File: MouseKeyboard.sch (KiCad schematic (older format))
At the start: 16 parts, among them IC1 ATMEGA328P-P, J1 USB, SW1 SW_PUSH, SW2 SW_PUSH, SW3 SW_PUSH, SW4 SW_PUSH, SW5 SW_PUSH, SW6 SW_PUSH, SW7 SW_PUSH

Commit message: Net File
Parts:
- R1: value R -> 2K2
- R2, R3: value R -> 68R
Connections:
- net +5V: now also IC1.20 (AVCC), IC1.7 (VCC), J1.1 (Vbus)
- net GND: no longer IC1.22 (GND), IC1.8 (GND)
- net at J1.3 (D+): now also D2.2 (K), R2.1
- no-connect marks 0 -> 17
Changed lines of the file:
@@
 EELAYER 24 0
 EELAYER END
-$Descr A4 11693 8268
+$Descr A 11000 8500
 encoding utf-8
 Sheet 1 1
-Title ""
-Date ""
+Title "Arduino Mouse Keyboard"
+Date "12 Feb 2015"
 Rev ""
 Comp ""
@@
 $EndComp
 $Comp
-L +5V #PWR6
-U 1 1 54DAA8BA
-P 9450 3400
-F 0 "#PWR6" H 9450 3490 20  0001 C CNN
-F 1 "+5V" H 9450 3490 30  0000 C CNN
-F 2 "" H 9450 3400 60  0000 C CNN
-F 3 "" H 9450 3400 60  0000 C CNN
-	1    9450 3400
-	1    0    0    -1
-$EndComp
-$Comp
-L +5V #PWR2
+L +5V #PWR01
 U 1 1 54DAA9EC
 P 1250 7150
-F 0 "#PWR2" H 1250 7240 20  0001 C CNN
+F 0 "#PWR01" H 1250 7240 20  0001 C CNN
 F 1 "+5V" H 1250 7240 30  0000 C CNN
 F 2 "" H 1250 7150 60  0000 C CNN
@@
 	1    1250 7150
 	0    -1   -1   0
-$EndComp
-$Comp
-L GND #PWR3
-U 1 1 54DAAA0D
-P 3850 7350
-F 0 "#PWR3" H 3850 7350 30  0001 C CNN
-F 1 "GND" H 3850 7280 30  0001 C CNN
-F 2 "" H 3850 7350 60  0000 C CNN
-F 3 "" H 3850 7350 60  0000 C CNN
-	1    3850 7350
-	1    0    0    -1
 $EndComp
 $Comp
@@
 $EndComp
 $Comp
-L GND #PWR1
-U 1 1 54DD39B5
-P 1200 5750
-F 0 "#PWR1" H 1200 5750 30  0001 C CNN
-F 1 "GND" H 1200 5680 30  0001 C CNN
-F 2 "" H 1200 5750 60  0000 C CNN
-F 3 "" H 1200 5750 60  0000 C CNN
-	1    1200 5750
-	1    0    0    -1
-$EndComp
-$Comp
 L USB J1
 U 1 1 54DD5132
@@
 P 6400 1900
 F 0 "R3" V 6480 1900 40  0000 C CNN
-F 1 "R" V 6407 1901 40  0000 C CNN
+F 1 "68R" V 6407 1901 40  0000 C CNN
 F 2 "" V 6330 1900 30  0000 C CNN
 F 3 "" H 6400 1900 30  0000 C CNN
@@
 P 6400 1650
 F 0 "R2" V 6480 1650 40  0000 C CNN
-F 1 "R" V 6407 1651 40  0000 C CNN
+F 1 "68R" V 6407 1651 40  0000 C CNN
 F 2 "" V 6330 1650 30  0000 C CNN
 F 3 "" H 6400 1650 30  0000 C CNN
@@
 $EndComp
 $Comp
-L +5V #PWR5
+L +5V #PWR02
 U 1 1 54DD56D2
 P 5850 1100
-F 0 "#PWR5" H 5850 1190 20  0001 C CNN
+F 0 "#PWR02" H 5850 1190 20  0001 C CNN
 F 1 "+5V" H 5850 1190 30  0000 C CNN
 F 2 "" H 5850 1100 60  0000 C CNN
@@
 P 5850 1400
 F 0 "R1" V 5930 1400 40  0000 C CNN
-F 1 "R" V 5857 1401 40  0000 C CNN
+F 1 "2K2" V 5857 1401 40  0000 C CNN
 F 2 "" V 5780 1400 30  0000 C CNN
 F 3 "" H 5850 1400 30  0000 C CNN
@@
 $EndComp
 $Comp
-L GND #PWR4
+L GND #PWR03
 U 1 1 54DD5A19
 P 5200 2550
-F 0 "#PWR4" H 5200 2550 30  0001 C CNN
+F 0 "#PWR03" H 5200 2550 30  0001 C CNN
 F 1 "GND" H 5200 2480 30  0001 C CNN
 F 2 "" H 5200 2550 60  0000 C CNN
@@
 Connection ~ 2200 7150
 Wire Wire Line
-	3850 6450 3850 7350
-Wire Wire Line
 	2700 6450 2700 7000
-Wire Wire Line
-	2700 7000 3850 7000
-Connection ~ 3850 7000
-Wire Wire Line
-	1200 5200 1200 5750
-Wire Wire Line
-	1200 5300 1600 5300
-Wire Wire Line
-	1600 5200 1200 5200
-Connection ~ 1200 5300
-Wire Wire Line
-	5850 1150 5850 1100
 Wire Wire Line
 	5850 1650 5850 1900
@@
 	6050 1650 6150 1650
 Wire Wire Line
+	6650 1650 7300 1650
+Wire Wire Line
+	6650 1900 7300 1900
+Wire Wire Line
+	3600 3950 3500 3950
+Wire Wire Line
+	3500 3850 3600 3850
+Wire Wire Line
+	2450 6200 2450 6300
+Wire Wire Line
+	3600 6300 3600 6200
+Wire Wire Line
+	3500 4800 3550 4800
+Wire Wire Line
+	3500 5300 3550 5300
+Wire Wire Line
+	8600 3500 4550 3500
+Wire Wire Line
+	4550 3500 4550 4900
+Wire Wire Line
+	4550 4900 3500 4900
+Wire Wire Line
+	3500 5000 4700 5000
+Wire Wire Line
+	4700 5000 4700 3800
+Wire Wire Line
+	4700 3800 8600 3800
+Wire Wire Line
+	3500 5100 4800 5100
+Wire Wire Line
+	4800 5100 4800 4100
+Wire Wire Line
+	4800 4100 8600 4100
+Wire Wire Line
+	3500 5200 5000 5200
+Wire Wire Line
+	5000 5200 5000 4450
+Wire Wire Line
+	5000 4450 8600 4450
+Wire Wire Line
+	3500 3100 7400 3100
+Wire Wire Line
+	7400 3100 7400 5100
+Wire Wire Line
+	7400 5100 8600 5100
+Wire Wire Line
+	3500 3200 7300 3200
+Wire Wire Line
+	7300 3200 7300 5400
+Wire Wire Line
+	7300 5400 8600 5400
+Wire Wire Line
+	3500 3000 7500 3000
+Wire Wire Line
+	7500 3000 7500 4750
+Wire Wire Line
+	7500 4750 8600 4750
+Wire Wire Line
+	1600 3000 1600 1700
+Wire Wire Line
+	1600 1700 4700 1700
+NoConn ~ 3500 3300
+NoConn ~ 3500 3400
+NoConn ~ 3500 3500
+NoConn ~ 3500 3600
+NoConn ~ 3500 3700
+NoConn ~ 3500 4700
+NoConn ~ 3500 4600
+NoConn ~ 3500 4450
+NoConn ~ 3500 4350
+NoConn ~ 3500 4250
+NoConn ~ 3500 4050
+NoConn ~ 3500 4150
+NoConn ~ 1600 3600
+Wire Wire Line
 	5450 1700 6050 1700
-Wire Wire Line
-	6650 1650 7300 1650
-Wire Wire Line
-	6650 1900 7300 1900
-Wire Wire Line
-	3600 3950 3500 3950
-Wire Wire Line
-	3500 3850 3600 3850
-Wire Wire Line
-	2450 6200 2450 6300
-Wire Wire Line
-	3600 6300 3600 6200
-Wire Wire Line
-	3500 4800 3550 4800
-Wire Wire Line
-	3500 5300 3550 5300
-Wire Wire Line
-	8600 3500 4550 3500
-Wire Wire Line
-	4550 3500 4550 4900
-Wire Wire Line
-	4550 4900 3500 4900
-Wire Wire Line
-	3500 5000 4700 5000
-Wire Wire Line
-	4700 5000 4700 3800
-Wire Wire Line
-	4700 3800 8600 3800
-Wire Wire Line
-	3500 5100 4800 5100
-Wire Wire Line
-	4800 5100 4800 4100
-Wire Wire Line
-	4800 4100 8600 4100
-Wire Wire Line
-	3500 5200 5000 5200
-Wire Wire Line
-	5000 5200 5000 4450
-Wire Wire Line
-	5000 4450 8600 4450
-Wire Wire Line
-	3500 3100 7400 3100
-Wire Wire Line
-	7400 3100 7400 5100
-Wire Wire Line
-	7400 5100 8600 5100
-Wire Wire Line
-	3500 3200 7300 3200
-Wire Wire Line
-	7300 3200 7300 5400
-Wire Wire Line
-	7300 5400 8600 5400
-Wire Wire Line
-	3500 3000 7500 3000
-Wire Wire Line
-	7500 3000 7500 4750
-Wire Wire Line
-	7500 4750 8600 4750
-Wire Wire Line
-	9450 3400 9450 5400
-Wire Wire Line
-	9450 3500 9200 3500
-Wire Wire Line
-	9450 3800 9200 3800
-Connection ~ 9450 3500
-Wire Wire Line
-	9450 4100 9200 4100
-Connection ~ 9450 3800
-Wire Wire Line
-	9450 4450 9200 4450
-Connection ~ 9450 4100
-Wire Wire Line
-	9450 4750 9200 4750
-Connection ~ 9450 4450
-Wire Wire Line
-	9450 5100 9200 5100
-Connection ~ 9450 4750
-Wire Wire Line
-	9450 5400 9200 5400
-Connection ~ 9450 5100
+Connection ~ 6050 1700
+NoConn ~ 5450 1950
+NoConn ~ 4700 1950
+$Comp
+L +5V #PWR04
+U 1 1 54DD6D39
+P 9550 3350
+F 0 "#PWR04" H 9550 3440 20  0001 C CNN
+F 1 "+5V" H 9550 3440 30  0000 C CNN
+F 2 "" H 9550 3350 60  0000 C CNN
+F 3 "" H 9550 3350 60  0000 C CNN
+	1    9550 3350
+	1    0    0    -1
+$EndComp
+Wire Wire Line
+	9200 3500 9550 3500
+Wire Wire Line
+	9550 3350 9550 5400
+Wire Wire Line
+	9550 3800 9200 3800
+Connection ~ 9550 3500
+Wire Wire Line
+	9550 4100 9200 4100
+Connection ~ 9550 3800
+Wire Wire Line
+	9550 4450 9200 4450
+Connection ~ 9550 4100
+Wire Wire Line
+	9550 4750 9200 4750
+Connection ~ 9550 4450
+Wire Wire Line
+	9550 5100 9200 5100
+Connection ~ 9550 4750
+Wire Wire Line
+	9550 5400 9200 5400
+Connection ~ 9550 5100
+Wire Wire Line
+	5850 1150 5850 1100
+$Comp
+L GND #PWR05
+U 1 1 54DD71C9
+P 1300 5600
+F 0 "#PWR05" H 1300 5600 30  0001 C CNN
+F 1 "GND" H 1300 5530 30  0001 C CNN
+F 2 "" H 1300 5600 60  0000 C CNN
+F 3 "" H 1300 5600 60  0000 C CNN
+	1    1300 5600
+	1    0    0    -1
+$EndComp
+Wire Wire Line
+	1300 5300 1300 5600
+NoConn ~ 1600 5200
+$Comp
+L +5V #PWR06
+U 1 1 54DD722E
+P 1300 3150
+F 0 "#PWR06" H 1300 3240 20  0001 C CNN
+F 1 "+5V" H 1300 3240 30  0000 C CNN
+F 2 "" H 1300 3150 60  0000 C CNN
+F 3 "" H 1300 3150 60  0000 C CNN
+	1    1300 3150
+	1    0    0    -1
+$EndComp
+Wire Wire Line
+	1300 3300 1600 3300
+Wire Wire Line
+	1300 3300 1300 3150
+Wire Wire Line
+	1500 3300 1500 3000
+Wire Wire Line
+	1500 3000 1600 3000
+Connection ~ 1500 3300
+Wire Wire Line
+	1450 5300 1450 7000
+Wire Wire Line
+	1450 7000 3850 7000
+Wire Wire Line
+	3850 7000 3850 6450
+Connection ~ 2700 7000
+Wire Wire Line
+	1300 5300 1450 5300
+NoConn ~ 1600 5300
 $EndSCHEMATC

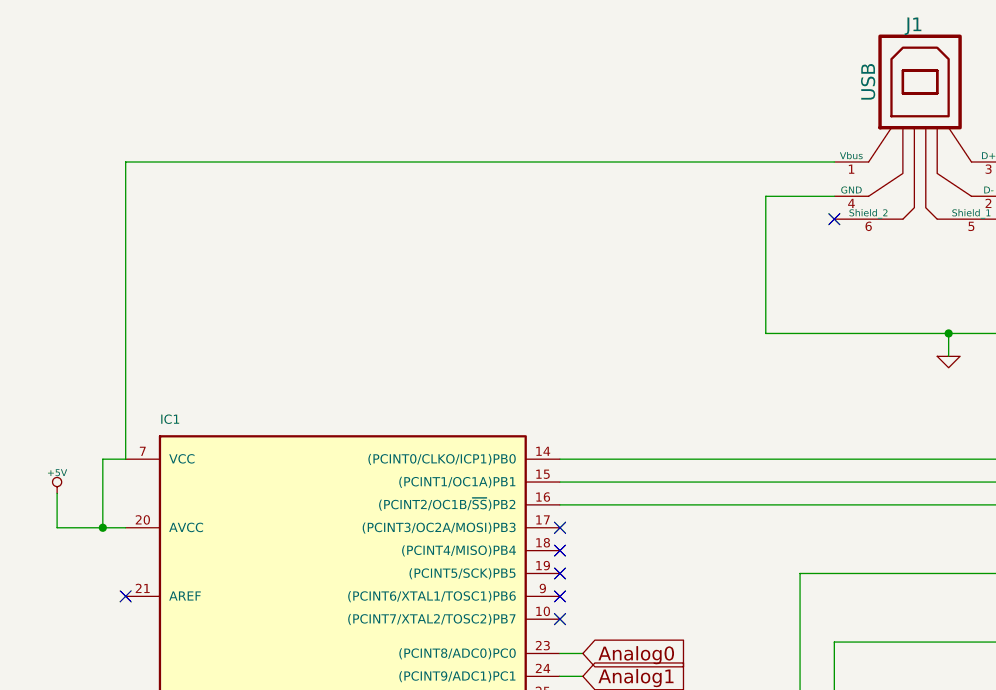
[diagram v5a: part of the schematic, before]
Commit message: Schematic Stuff
* Moved some wires
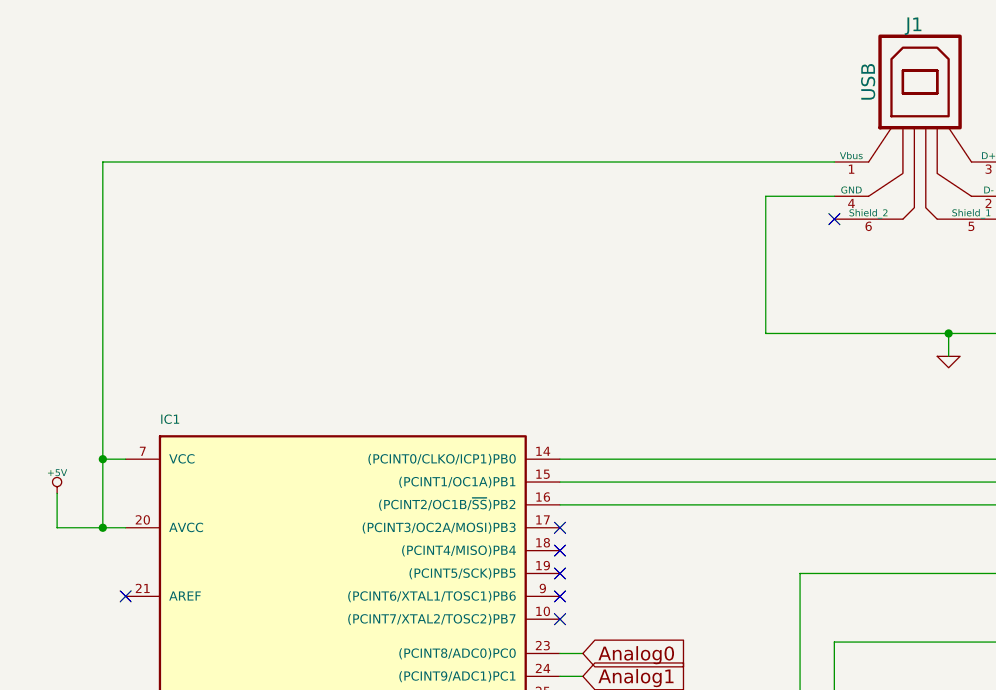
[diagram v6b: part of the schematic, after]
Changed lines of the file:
@@
 	7500 4750 8600 4750
 Wire Wire Line
-	1600 3000 1600 1700
-Wire Wire Line
-	1600 1700 4700 1700
+	1500 1700 4700 1700
 NoConn ~ 3500 3300
 NoConn ~ 3500 3400
@@
 	1300 3300 1300 3150
 Wire Wire Line
-	1500 3300 1500 3000
+	1500 1700 1500 3300
 Wire Wire Line
 	1500 3000 1600 3000
@@
 	1300 5300 1450 5300
 NoConn ~ 1600 5300
+Connection ~ 1500 3000
 $EndSCHEMATC

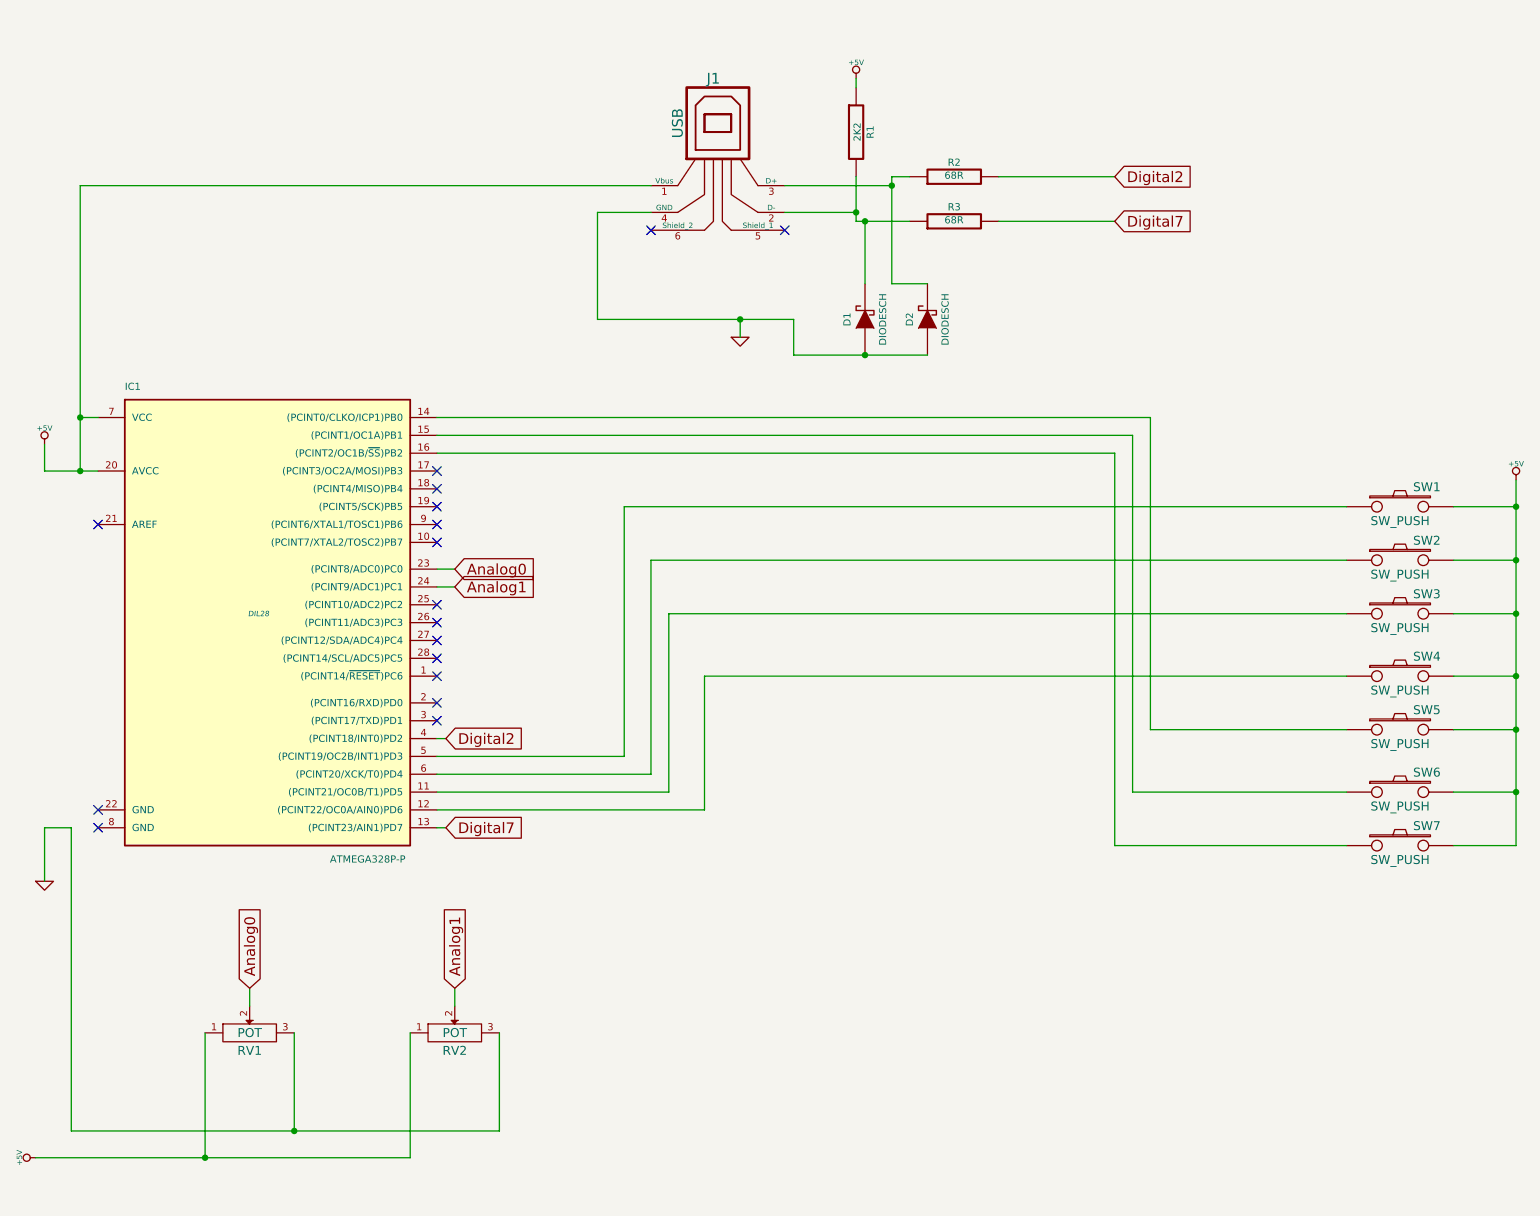
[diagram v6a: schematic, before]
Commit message: My schematic was terrible
It's being redrawn by me
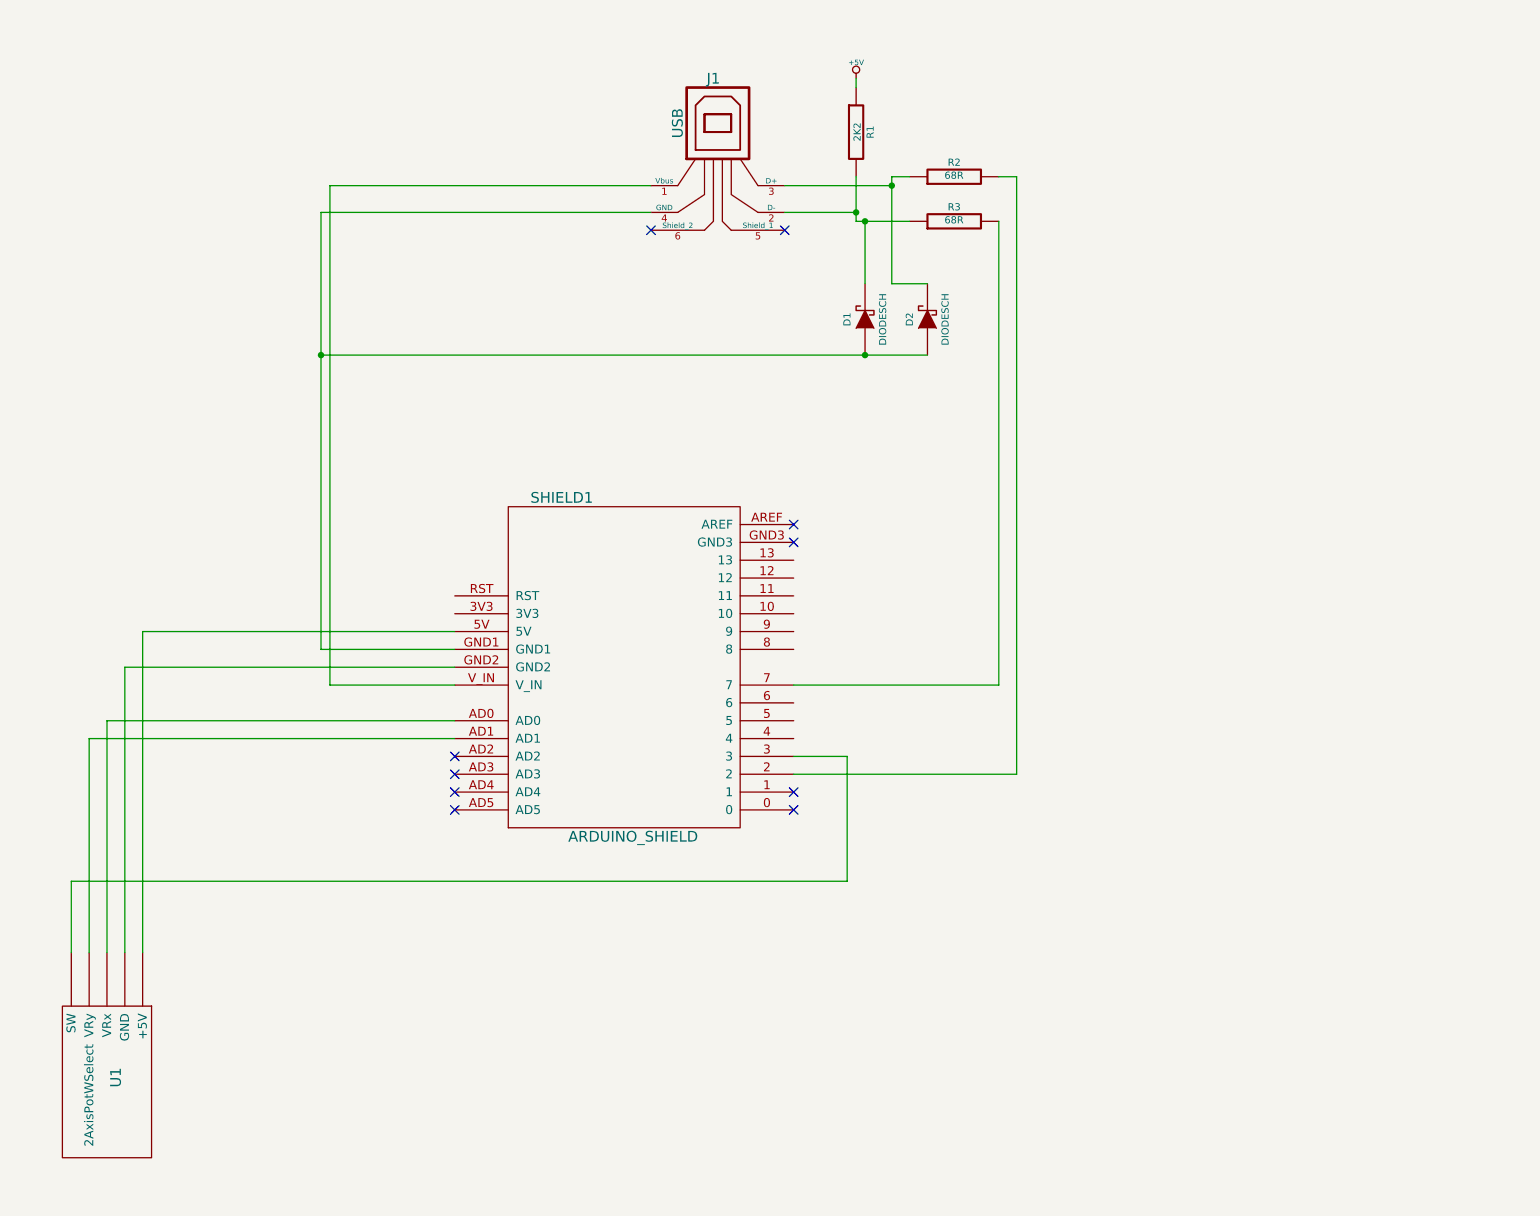
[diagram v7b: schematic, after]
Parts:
- removed IC1: ATMEGA328P-P, DIL28, symbol ATMEGA328P-P
- removed RV1, RV2: POT, symbol POT
- removed SW1, SW2, SW3, SW4, SW5, SW6, SW7: SW_PUSH, symbol SW_PUSH
- added SHIELD1: ARDUINO_SHIELD, symbol ARDUINO_SHIELD
- added U1: 2AxisPotWSelect, symbol 2AxisPotWSelect
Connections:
- net +5V: no longer J1.1 (Vbus)
- net Digital2: no longer names the net of R2.2
- net Digital2: now also SHIELD1.2
- net Digital7: no longer names the net of R3.2
- net Digital7: now also SHIELD1.7
- net GND: no longer names the net of D1.1 (A), D2.1 (A), J1.4 (GND)
- net GND: now also SHIELD1.GND1
- new net: J1.1 (Vbus), SHIELD1.V_IN
- new net: SHIELD1.3, U1.~ (VRy)
- new net: SHIELD1.5V, U1.~ (VRy)
- new net: SHIELD1.AD0, U1.~ (VRy)
- new net: SHIELD1.AD1, U1.~ (VRy)
- new net: SHIELD1.GND2, U1.~ (VRy)
- no-connect marks 17 -> 10
